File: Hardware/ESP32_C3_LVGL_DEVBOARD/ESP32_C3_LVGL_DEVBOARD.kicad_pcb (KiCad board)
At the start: 4 copper layers, 27 x 40 mm, 66 parts, among them J1 CONN_USBC, J2 CONN_UART, J3 Conn_Coaxial, SW1 SW_Push_SPST_4Pads, SW2 SW_Push_SPST_4Pads, U2 USBLC6-2SC6, U3 AMS1117-3.3, U4 ESP32-C3, U5 Winbond-W25Q64JVSSIQ, U6 USBLC6-2SC6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

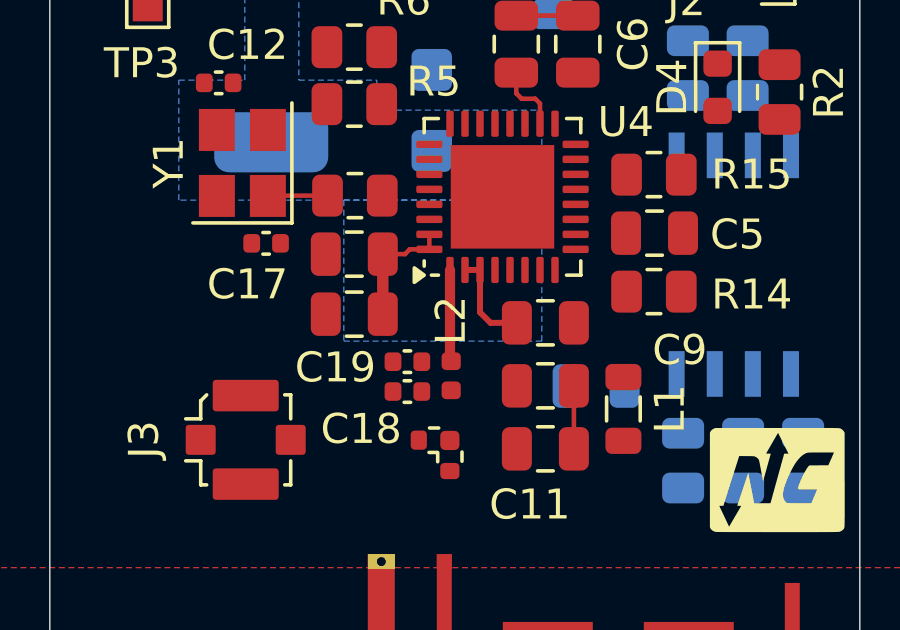
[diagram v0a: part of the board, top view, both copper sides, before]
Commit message: updated pcb build up details
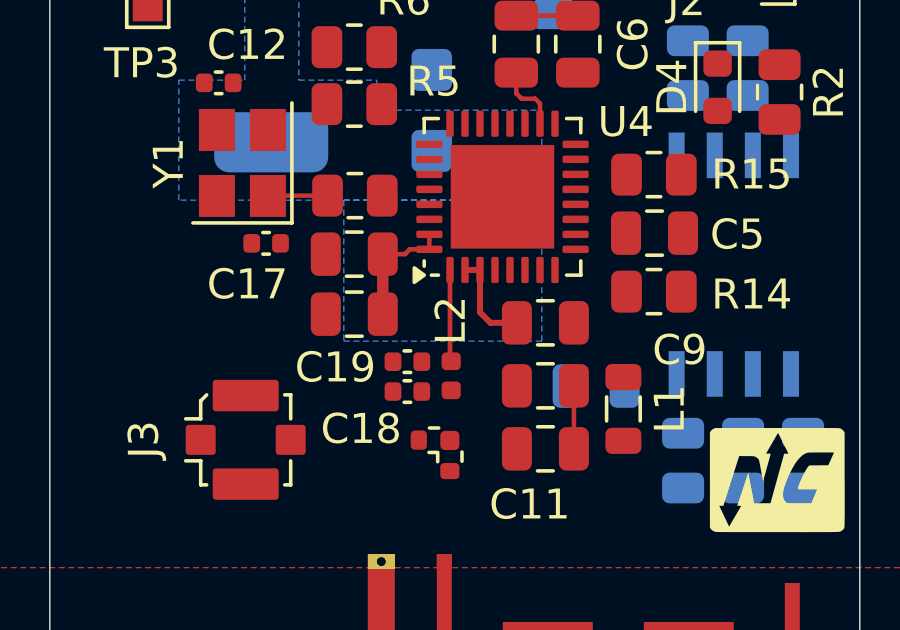
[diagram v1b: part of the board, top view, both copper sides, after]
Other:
- board text added: "0.0994 mm"
- board text added: "1.265 mm"
- board text added: "4.1"
- board text added: "4.6"
- board text added: "Dielectric 1"
- board text added: "Dielectric 2"
- board text added: "Dielectric 3"
- board text added: "https://jlcpcb.com/impedance 4 Layer Impedance Controlled Stackup Standard 3313 Stackup Thichness: 1.6mm Outer Cu Weight: 1oz Inner Cu Weight: 0.5oz L1 - SIGNAL + ROUTED PWR L2 - GND L3 - GND L4 - SIGNAL + ROUTED PWR"
- board text removed: "0.2104 mm"
- board text removed: "1.065 mm"
- board text removed: "4.5"
- board text removed: "Dielectric"
- board text removed: "https://jlcpcb.com/impedance 4 Layer Impedance Controlled Stackup Standard No requirement Stackup / 7628 Stackup Thichness: 1.6mm Outer Cu Weight: 1oz Inner Cu Weight: 0.5oz L1 - SIGNAL + ROUTED PWR L2 - GND L3 - GND L4 - SIGNAL + ROUTED PWR"

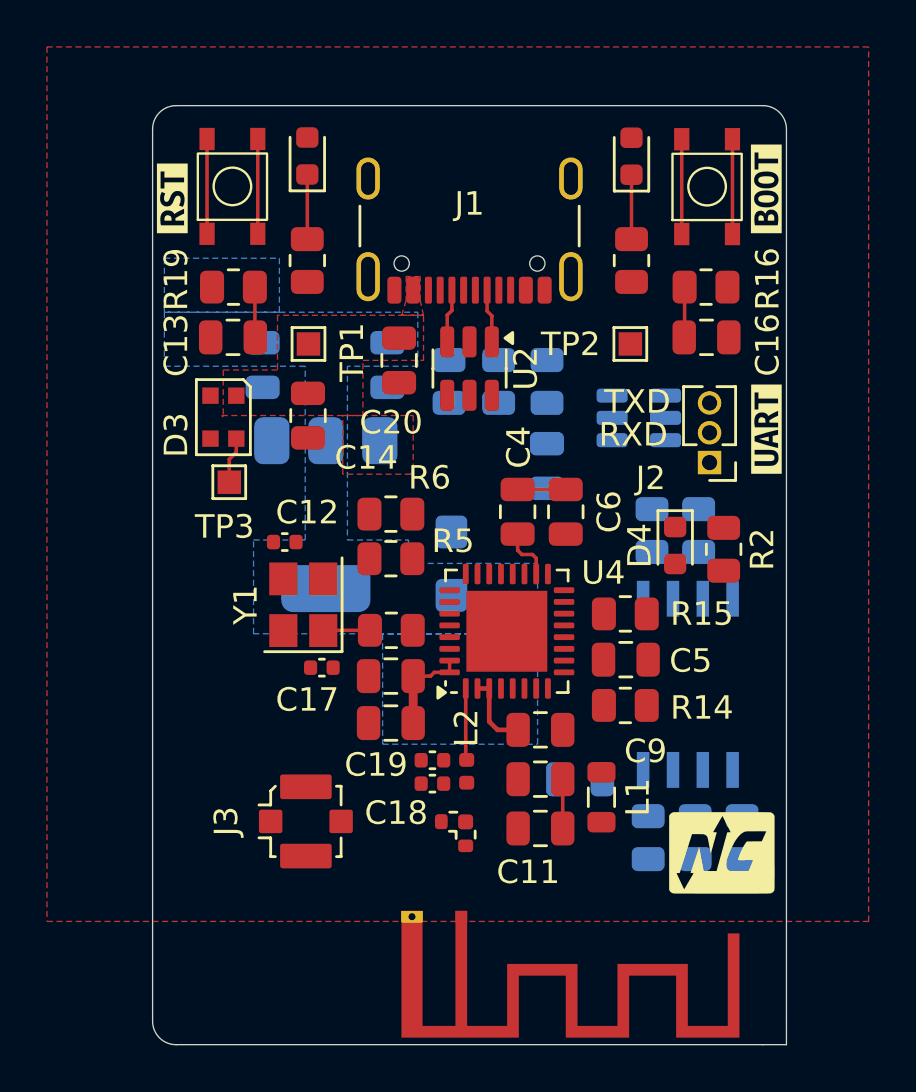
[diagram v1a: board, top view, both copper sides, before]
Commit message: updated pcb with placement & basic routing
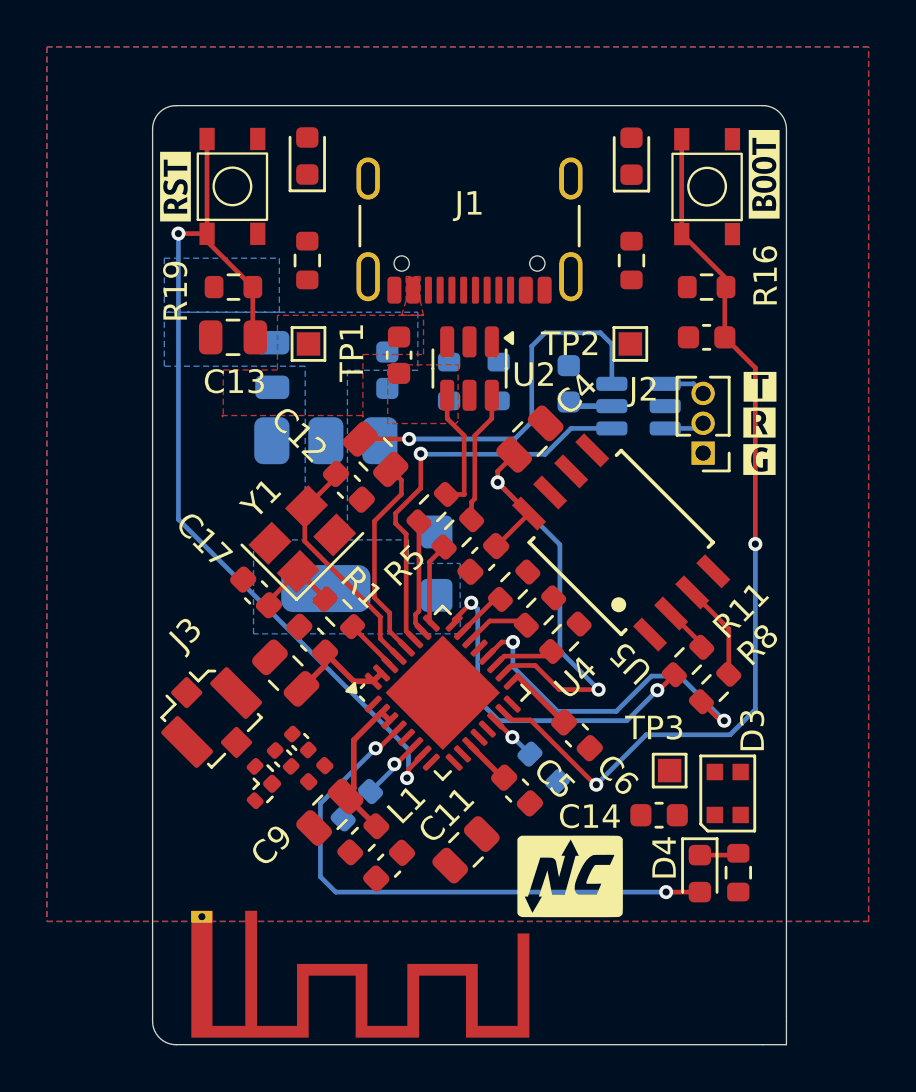
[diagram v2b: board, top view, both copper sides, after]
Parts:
- removed kibuzzard-677039AB: G***, kibuzzard-677039AB
- added kibuzzard-67796362: G***, kibuzzard-67796362, F.Cu at (166.4, 77.5)
- added kibuzzard-67796372: G***, kibuzzard-67796372, F.Cu at (166.3, 79.0)
- added kibuzzard-6779637F: G***, kibuzzard-6779637F, F.Cu at (166.3, 80.6)
- C10, C14, C16, C20, C21, C3, C5, C6, C7: footprint Capacitor_SMD:C_0805_2012Metric -> Capacitor_SMD:C_0603_1608Metric
- C12, C17: footprint Capacitor_SMD:C_0402_1005Metric -> Capacitor_SMD:C_0603_1608Metric
- C15: footprint Capacitor_SMD:C_0805_2012Metric -> Capacitor_SMD:C_0603_1608Metric; moved to F.Cu
- D4: value LED_G -> LED_B
- L1: footprint Inductor_SMD:L_0805_2012Metric -> Inductor_SMD:L_0603_1608Metric
- R1, R12, R13, R16, R19, R2, R3, R4, R5, R6: footprint Resistor_SMD:R_0805_2012Metric -> Resistor_SMD:R_0603_1608Metric
- R10, R11, R7, R8, R9: footprint Resistor_SMD:R_0805_2012Metric -> Resistor_SMD:R_0603_1608Metric; moved to F.Cu
- R14, R15: footprint Resistor_SMD:R_0805_2012Metric -> Resistor_SMD:R_0603_1608Metric; moved to B.Cu
- R17, U5: moved to F.Cu
- moved D3 26.8 mm to (165.0, 94.8), turned to 90 degrees
- moved C14 22.7 mm to (162.1, 95.7), turned to 180 degrees
- moved TP3 22.4 mm to (162.5, 93.8)
- moved R10 14.5 mm to (155.9, 86.0), turned to -135 degrees
- moved D4 14.0 mm to (163.8, 98.2)
- moved R2 13.8 mm to (165.4, 98.2)
- moved R14 12.2 mm to (149.2, 95.3), turned to -135 degrees
- moved R9 11.7 mm to (157.0, 87.0), turned to -135 degrees
- moved L1 10.3 mm to (149.5, 96.8), turned to 45 degrees
- moved C15 10.3 mm to (154.6, 84.8), turned to -135 degrees
- moved C9 9.63 mm to (148.1, 95.6), turned to -135 degrees
- moved C6 9.53 mm to (158.6, 92.3), turned to -45 degrees
- moved R7 9.22 mm to (158.1, 88.2), turned to -135 degrees
- moved ANT1 8.95 mm to (144.7, 100.0)
- moved R17 7.93 mm to (150.0, 80.3), turned to 135 degrees
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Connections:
- net Net-(U4-GPIO18/USB_D-) renamed /USB_PART-
- net Net-(U4-GPIO19/USB_D+) renamed /USB_PART+
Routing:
- net /ESP_RST: track 6.19 -> 39.1 mm, vias 0 -> 2
- net Net-(U4-GPIO9/BOOT): track 6.19 -> 38.9 mm, vias 0 -> 2
- net /USER_LED: track 0.00 -> 24.2 mm, vias 0 -> 2
- net VDD_SPI: track 2.29 -> 20.5 mm, vias 0 -> 2
- net Net-(U4-U0RXD/GPIO20): track 0.00 -> 17.3 mm, vias 0 -> 1
- net Net-(R17-Pad2): track 0.00 -> 16.4 mm, vias 0 -> 1
- net Net-(U4-SPIQ/GPIO17): track 0.00 -> 15.0 mm, vias 0 -> 2
- net Net-(U4-SPIWP/GPIO13): track 0.00 -> 14.9 mm, vias 0 -> 2
- net +3V3: track 7.41 -> 18.6 mm
- net Net-(U4-XTAL_N): track 0.00 -> 9.97 mm
- net GND: track 10.1 -> 0.74 mm
- net Net-(U4-U0TXD/GPIO21): track 0.00 -> 8.84 mm
- net /USB_D-: track 0.00 -> 5.66 mm
- net /USB_D+: track 0.00 -> 5.29 mm
- net /USB_PART+: track 0.00 -> 4.86 mm
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- added copper zone on B.Cu, net GND
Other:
- board text removed: "RXD"
- board text removed: "TXD"

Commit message: kicad project update
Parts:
- moved kibuzzard-6771D0B9 14.7 mm to (166.1, 74.8), turned to 90 degrees
- moved ANT1 4.75 mm to (149.4, 100.0)
- moved R10 0.18 mm to (155.8, 85.8)
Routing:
- net +3V3: track 18.6 -> 92.0 mm, vias 0 -> 7
- net VBUS: track 0.00 -> 63.4 mm, vias 0 -> 2
- net /WS2812B: track 0.00 -> 9.83 mm
- net /SPICS0: track 0.00 -> 9.40 mm, vias 0 -> 2
- net /SPIHD: track 0.00 -> 8.22 mm, vias 0 -> 2
- net Net-(J1-CC2): track 0.00 -> 7.85 mm, vias 0 -> 1
- net /SPICLK: track 0.00 -> 7.64 mm, vias 0 -> 2
- net Net-(ANT1-ANT): track 0.00 -> 7.53 mm
- net /SPID: track 0.00 -> 7.52 mm
- net Net-(J1-D--PadA7): track 0.00 -> 7.01 mm
- net Net-(J1-CC1): track 0.00 -> 7.00 mm, vias 0 -> 1
- net GND: track 0.74 -> 7.09 mm, vias 0 -> 88
- net Net-(J1-D+-PadA6): track 0.00 -> 6.06 mm, vias 0 -> 2
- net Net-(C10-Pad1): track 0.00 -> 4.96 mm
- net Net-(U4-LNA_IN): track 0.00 -> 4.46 mm
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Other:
- outline, holes or cut-outs redrawn

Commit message: pcb commit
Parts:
- moved C10 0.62 mm to (151.0, 97.4)
- moved L1 0.62 mm to (149.9, 96.3)
- moved C9 0.62 mm to (148.5, 95.2)
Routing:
- net Net-(U4-SPIWP/GPIO13): track 14.9 -> 15.8 mm
- net GND: vias 88 -> 100
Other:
- board text added: "https://jlcpcb.com/impedance 4 Layer Impedance Controlled Stackup Standard 3313 Stackup (JLC04161H-3313(Finished thickness1.56mm±10%)) Thichness: 1.6mm Outer Cu Weight: 1oz Inner Cu Weight: 0.5oz L1 - SIGNAL + ROUTED PWR L2 - GND L3 - GND L4 - SIGNAL + ROUTED PWR"
- board text removed: "https://jlcpcb.com/impedance 4 Layer Impedance Controlled Stackup Standard 3313 Stackup Thichness: 1.6mm Outer Cu Weight: 1oz Inner Cu Weight: 0.5oz L1 - SIGNAL + ROUTED PWR L2 - GND L3 - GND L4 - SIGNAL + ROUTED PWR"

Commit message: pcb project update
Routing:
- net GND: vias 100 -> 127

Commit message: updated pcb + gerbers+ drills
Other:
- rule pad_to_mask_clearance: 0.05 -> 0
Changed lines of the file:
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@@
 			(dielectric_constraints yes)
 		)
-		(pad_to_mask_clearance 0.05)
-		(solder_mask_min_width 0.1)
+		(pad_to_mask_clearance 0)
 		(allow_soldermask_bridges_in_footprints no)
 		(pcbplotparams
 			(layerselection 0x00010fc_ffffffff)
-			(plot_on_all_layers_selection 0x0000000_00000000)
+			(plot_on_all_layers_selection 0x00010fc_80000007)
 			(disableapertmacros no)
-			(usegerberextensions no)
-			(usegerberattributes yes)
-			(usegerberadvancedattributes yes)
-			(creategerberjobfile yes)
+			(usegerberextensions yes)
+			(usegerberattributes no)
+			(usegerberadvancedattributes no)
+			(creategerberjobfile no)
 			(dashed_line_dash_ratio 12.000000)
 			(dashed_line_gap_ratio 3.000000)
@@
 			(psa4output no)
 			(plotreference yes)
-			(plotvalue yes)
+			(plotvalue no)
 			(plotfptext yes)
 			(plotinvisibletext no)
 			(sketchpadsonfab no)
-			(subtractmaskfromsilk no)
+			(subtractmaskfromsilk yes)
 			(outputformat 1)
 			(mirror no)
-			(drillshape 1)
+			(drillshape 0)
 			(scaleselection 1)
-			(outputdirectory "")
+			(outputdirectory "../JLPCB Exports/")
 		)
 	)
